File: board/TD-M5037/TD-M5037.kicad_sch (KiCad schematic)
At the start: 25 parts, among them J1 Pin 1x6, J2 Pin 1x5, J3 AVR-ISP, J5 Pin 1x6, J5 PowerPad, J8 PowerPad, U2 DS1307, U3 ATmega328PB-QFP, Y1 16MHz, Y1 32.768KHz

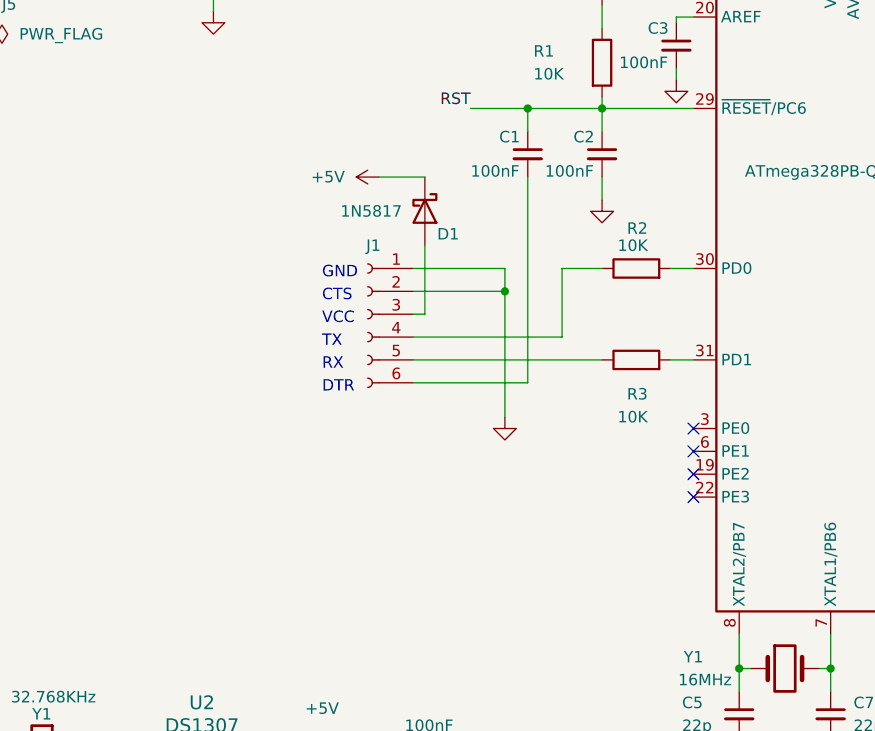
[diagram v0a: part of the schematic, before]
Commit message: Add diagnostic heartbeat
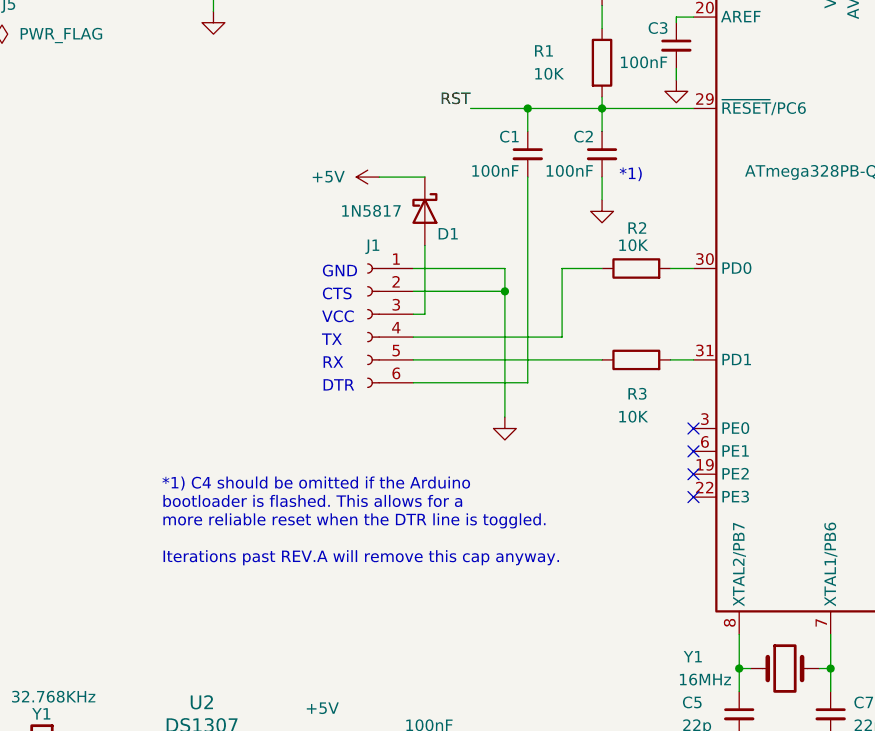
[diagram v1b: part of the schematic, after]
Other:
- note added: "*1)"
- note added: "*1) C4 should be omitted if the Arduino bootloader is flashed. This allows for a more reliable reset when the DTR line is toggled. Iterations past REV.A will remove this cap anyway."
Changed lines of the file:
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@@
     (stroke (width 0) (type default))
+  )
+  (text "*1) C4 should be omitted if the Arduino \nbootloader is flashed. This allows for a\nmore reliable reset when the DTR line is toggled.\n\nIterations past REV.A will remove this cap anyway."
+    (at 55.88 111.76 0)
+    (effects (font (size 1.27 1.27)) (justify left bottom))
+  )
+  (text "*1)" (at 106.68 69.215 0)
+    (effects (font (size 1.27 1.27)) (justify left bottom))
   )
   (text "RX" (at 73.66 90.17 0)

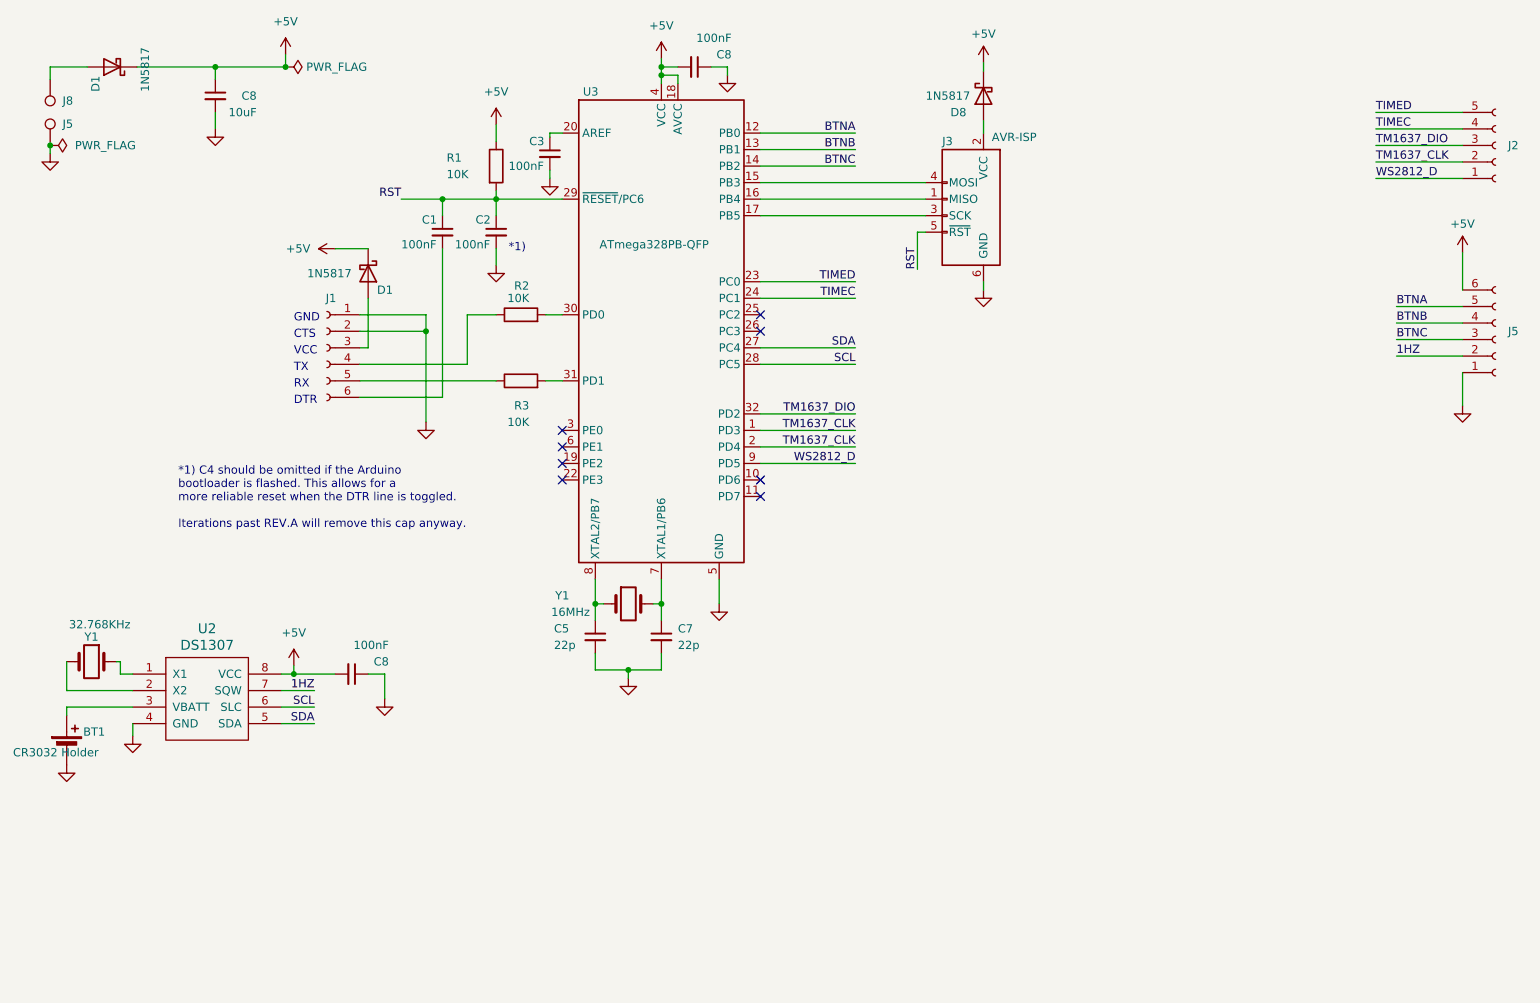
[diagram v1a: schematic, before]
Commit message: Fix FACE_ID undefined
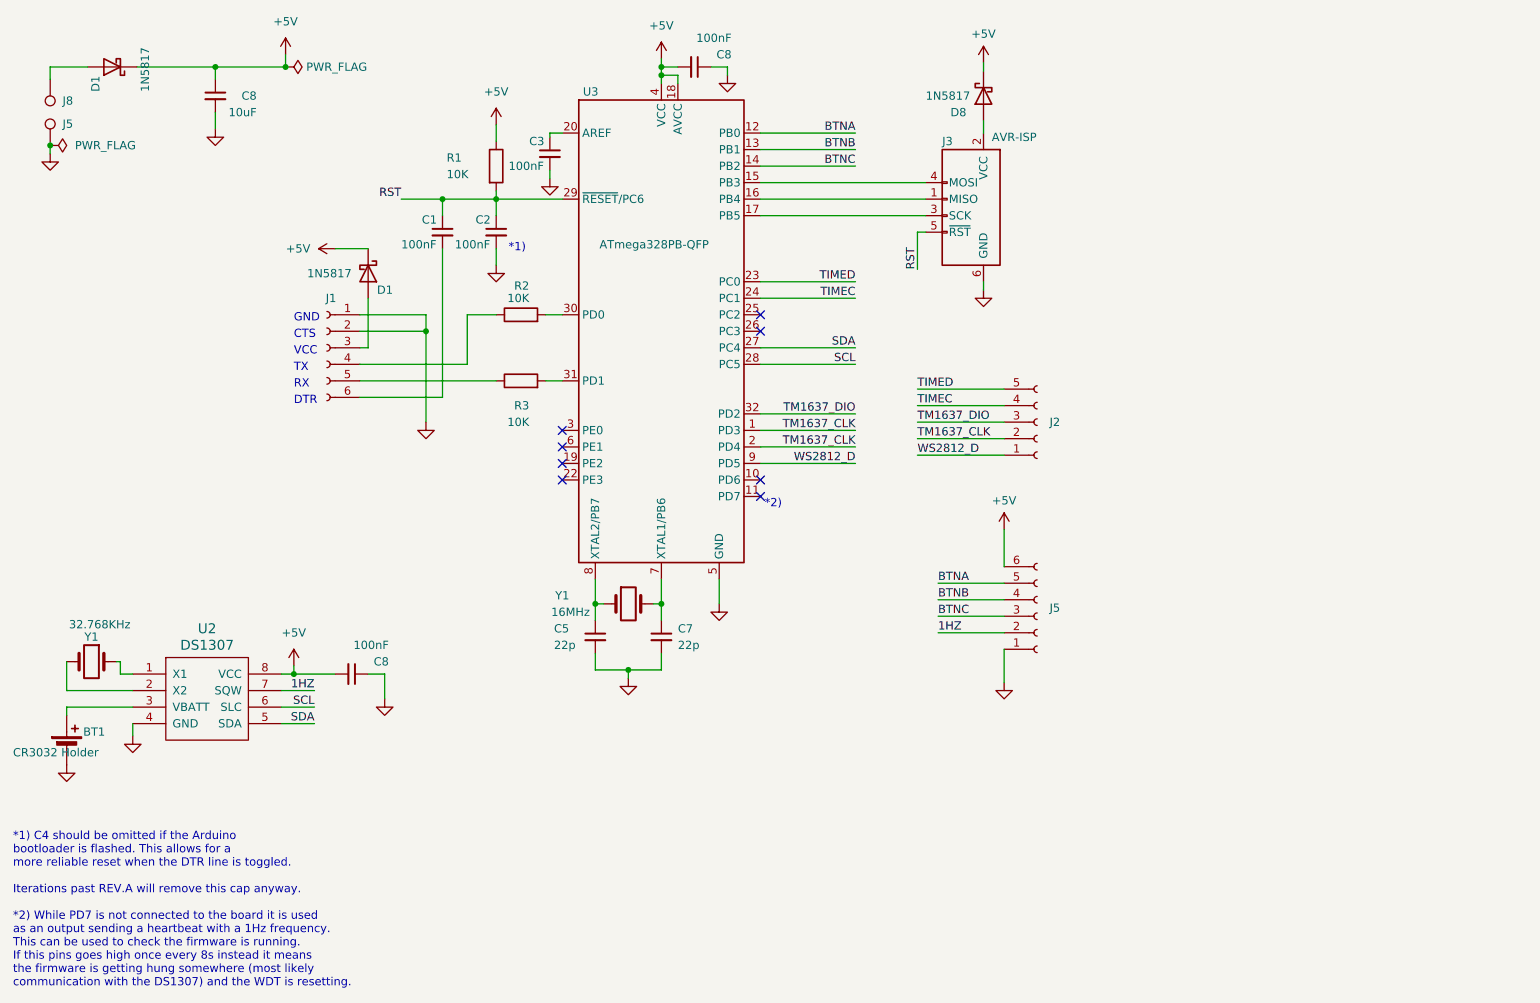
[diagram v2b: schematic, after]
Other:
- note added: "*1) C4 should be omitted if the Arduino bootloader is flashed. This allows for a more reliable reset when the DTR line is toggled. Iterations past REV.A will remove this cap anyway. *2) While PD7 is not connected to the board it is used as an output sending a heartbeat with a 1Hz frequency. This can be used to check the firmware is running. If this pins goes high once every 8s instead it means th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"
- note added: "*2)"
- note removed: "*1) C4 should be omitted if the Arduino bootloader is flashed. This allows for a more reliable reset when the DTR line is toggled. Iterations past REV.A will remove this cap anyway."
- moved on the sheet: J2, J5

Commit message: Prepare for sale
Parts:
- renumbered C5 to C1, C7 to C2, C1 to C3, C2 to C4, C3 to C5, C8 to C6, C8 to C7, D1 to D2, D8 to D3, J2 to J1, J5 to J4, J1 to J6, J3 to J7, Y1 to Y2
